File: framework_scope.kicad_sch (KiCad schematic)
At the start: 0 parts

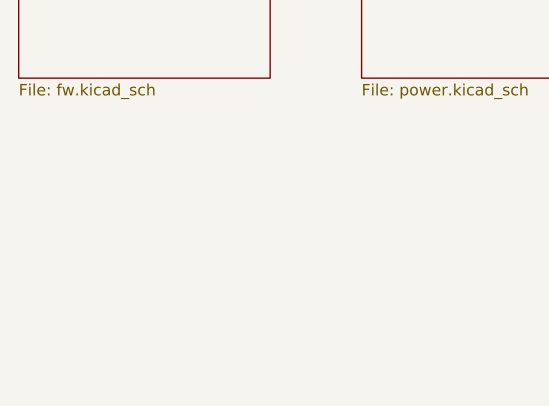
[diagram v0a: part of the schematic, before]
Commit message: added adc
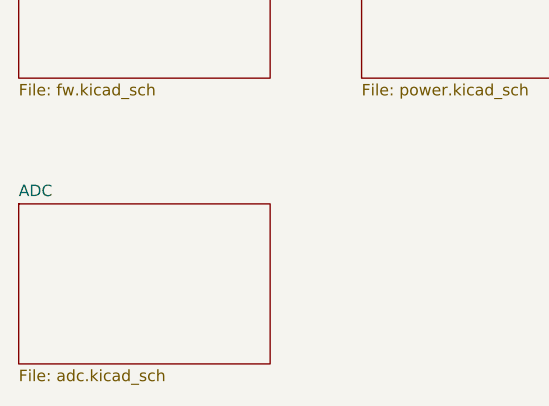
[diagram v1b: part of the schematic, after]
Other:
- added sheet ADC (adc.kicad_sch)
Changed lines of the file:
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@@
+	)
+	(sheet
+		(at 21.59 57.15)
+		(size 27.94 17.78)
+		(exclude_from_sim no)
+		(in_bom yes)
+		(on_board yes)
+		(dnp no)
+		(fields_autoplaced yes)
+		(stroke
+			(width 0.1524)
+			(type solid)
+		)
+		(fill
+			(color 0 0 0 0)
+		)
+		(property "Sheetname" "ADC"
+			(at 21.59 56.4384 0)
+			(show_name no)
+			(do_not_autoplace no)
+			(effects
+				(font
+					(size 1.27 1.27)
+				)
+				(justify left bottom)
+			)
+		)
+		(property "Sheetfile" "adc.kicad_sch"
+			(at 21.59 75.5146 0)
+			(show_name no)
+			(do_not_autoplace no)
+			(effects
+				(font
+					(size 1.27 1.27)
+				)
+				(justify left top)
+			)
+		)
+		(property "Field2" ""
+			(at 21.59 57.15 0)
+			(hide yes)
+			(show_name no)
+			(do_not_autoplace no)
+			(effects
+				(font
+					(size 1.27 1.27)
+				)
+			)
+		)
+		(instances
+			(project "framework_scope"
+				(path "/f3d50a77-3de6-40a4-8981-4f0500943bc1"
+					(page "6")
+				)
+			)
+		)
 	)
 	(sheet

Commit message: added clk
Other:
- sheet ADC renamed ADC 1
- added sheet ADC 2 (adc_2.kicad_sch)
- added sheet Clock (clk.kicad_sch)
- sheet ADC 1: file adc.kicad_sch -> adc_1.kicad_sch
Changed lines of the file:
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@@
 			(color 0 0 0 0)
 		)
-		(property "Sheetname" "ADC"
+		(property "Sheetname" "ADC 1"
 			(at 21.59 56.4384 0)
 			(show_name no)
@@
 			)
 		)
-		(property "Sheetfile" "adc.kicad_sch"
+		(property "Sheetfile" "adc_1.kicad_sch"
 			(at 21.59 75.5146 0)
 			(show_name no)
@@
 	)
 	(sheet
+		(at 95.25 57.15)
+		(size 29.21 17.78)
+		(exclude_from_sim no)
+		(in_bom yes)
+		(on_board yes)
+		(dnp no)
+		(fields_autoplaced yes)
+		(stroke
+			(width 0.1524)
+			(type solid)
+		)
+		(fill
+			(color 0 0 0 0)
+		)
+		(property "Sheetname" "ADC 2"
+			(at 95.25 56.4384 0)
+			(show_name no)
+			(do_not_autoplace no)
+			(effects
+				(font
+					(size 1.27 1.27)
+				)
+				(justify left bottom)
+			)
+		)
+		(property "Sheetfile" "adc_2.kicad_sch"
+			(at 95.25 75.5146 0)
+			(show_name no)
+			(do_not_autoplace no)
+			(effects
+				(font
+					(size 1.27 1.27)
+				)
+				(justify left top)
+			)
+		)
+		(instances
+			(project "framework_scope"
+				(path "/f3d50a77-3de6-40a4-8981-4f0500943bc1"
+					(page "7")
+				)
+			)
+		)
+	)
+	(sheet
 		(at 95.25 22.86)
 		(size 29.21 20.32)
@@
 				)
 			)
+		)
+	)
+	(sheet
+		(at 59.69 57.15)
+		(size 27.94 17.78)
+		(exclude_from_sim no)
+		(in_bom yes)
+		(on_board yes)
+		(dnp no)
+		(fields_autoplaced yes)
+		(stroke
+			(width 0.1524)
+			(type solid)
+		)
+		(fill
+			(color 0 0 0 0)
+		)
+		(property "Sheetname" "Clock"
+			(at 59.69 56.4384 0)
+			(show_name no)
+			(do_not_autoplace no)
+			(effects
+				(font
+					(size 1.27 1.27)
+				)
+				(justify left bottom)
+			)
+		)
+		(property "Sheetfile" "clk.kicad_sch"
+			(at 59.69 75.5146 0)
+			(show_name no)
+			(do_not_autoplace no)
+			(effects
+				(font
+					(size 1.27 1.27)
+				)
+				(justify left top)
+			)
+		)
+		(instances
+			(project "framework_scope"
+				(path "/f3d50a77-3de6-40a4-8981-4f0500943bc1"
+					(page "8")
+				)
+			)
